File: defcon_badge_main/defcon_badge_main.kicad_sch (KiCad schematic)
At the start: 2 parts, among them U1 TPS61023DRLR, U2 TPS61023DRLR

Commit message: progress from 2_21_26
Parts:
- removed U1, U2: TPS61023DRLR, TPS61023DRLR:SOT563-ORI, symbol TPS61023DRLR:TPS61023DRLR
- added BT1: Battery, symbol Device:Battery
- added J2: ~, joystick:joystick, symbol joystick:joystick
- added M1, M2, M3: Stepper_Motor_bipolar, symbol Motor:Stepper_Motor_bipolar
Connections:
- net GND: now also BT1.2 (-)
- new net 3v3_power/VBAT: BT1.1 (+)
- new net motor_driver/OUT1A: M1.2 (-)
- new net motor_driver/OUT1B: M1.1
- new net motor_driver/OUT2A: M1.3
- new net motor_driver/OUT2B: M1.4
- new net motor_driver1/OUT1A: M2.2 (-)
- new net motor_driver1/OUT1B: M2.1
- new net motor_driver1/OUT2A: M2.3
- new net motor_driver1/OUT2B: M2.4
- new net motor_driver2/OUT1A: M3.2 (-)
- new net motor_driver2/OUT1B: M3.1
- new net motor_driver2/OUT2A: M3.3
- new net motor_driver2/OUT2B: M3.4
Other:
- added sheet 3v3_power (power_regulator.kicad_sch)
- added sheet 5v_power (power_reg_5v.kicad_sch)
- added sheet esp32 (esp32.kicad_sch)
- added sheet motor_driver (motor_drivers.kicad_sch)
- added sheet motor_driver1 (motor_drivers.kicad_sch)
- added sheet motor_driver2 (motor_drivers.kicad_sch)

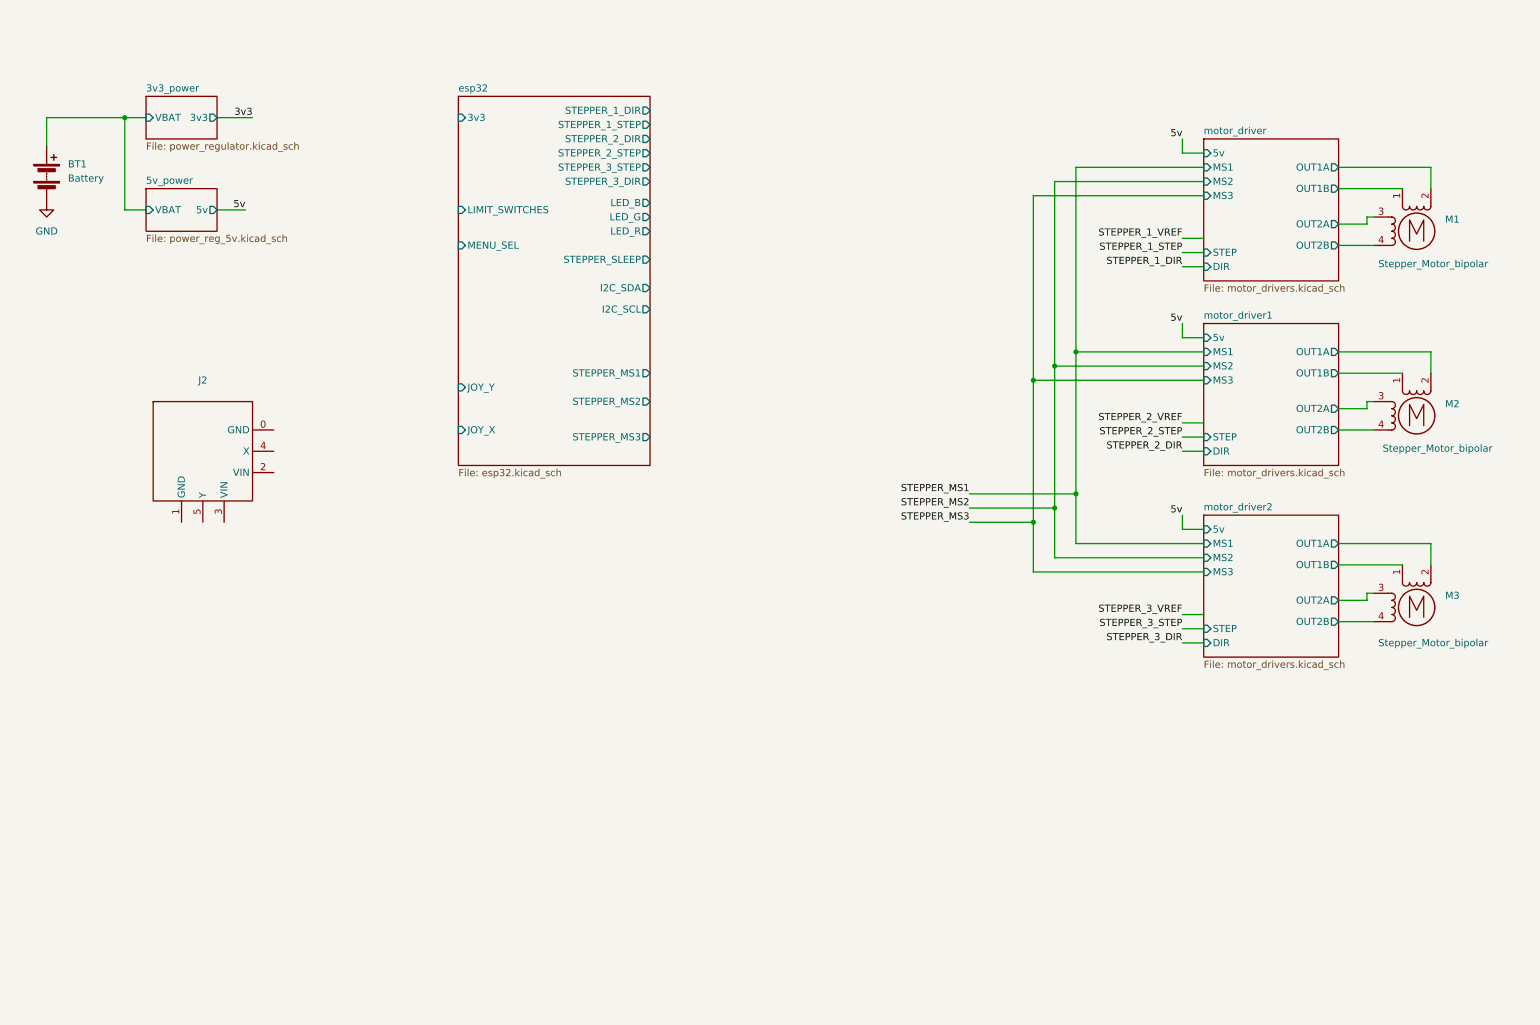
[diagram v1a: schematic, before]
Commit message: ESP32 test board layout
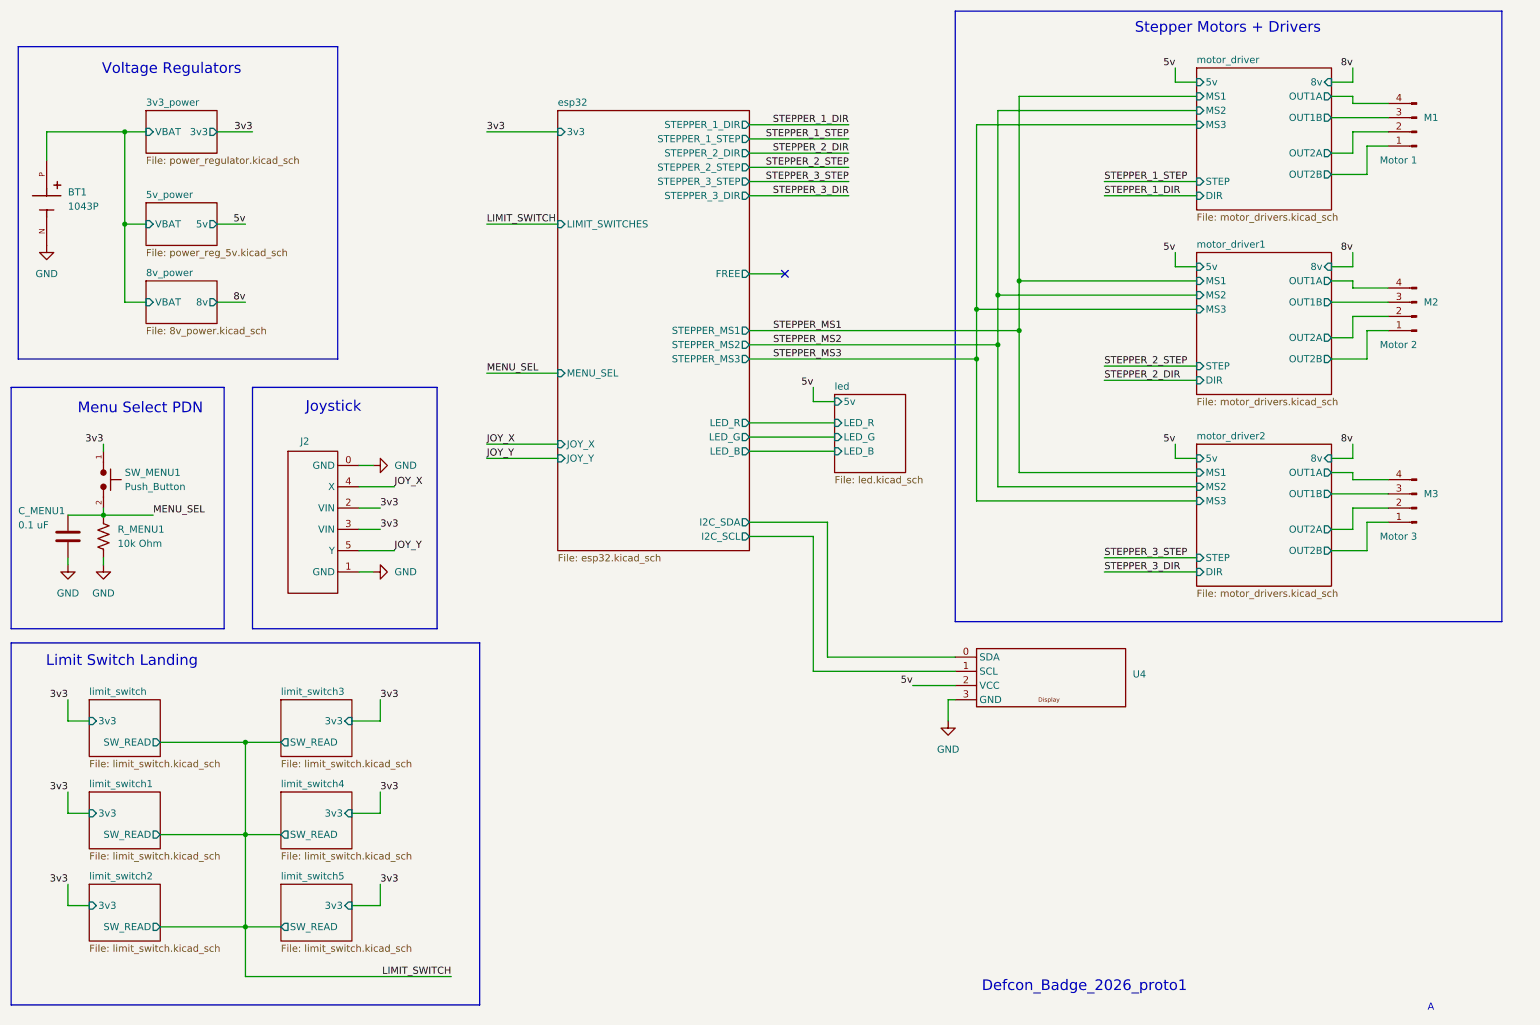
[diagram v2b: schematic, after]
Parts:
- removed BT1: Battery, symbol Device:Battery
- removed M1, M2, M3: Stepper_Motor_bipolar, symbol Motor:Stepper_Motor_bipolar
- added BT1: 1043P, 1043P:BAT_1043P, symbol 1043P:1043P
- added C_MENU1: 0.1 uF, PCM_SparkFun-Coil:0805, symbol Device:C
- added M1: Motor 1, joystick:motor_pins, symbol Connector:Conn_01x04_Pin
- added M2: Motor 2, joystick:motor_pins, symbol Connector:Conn_01x04_Pin
- added M3: Motor 3, joystick:motor_pins, symbol Connector:Conn_01x04_Pin
- added R_MENU1: 10k Ohm, PCM_SparkFun-Coil:0805, symbol Device:R_US
- added SW_MENU1: Push_Button, Button_Switch_SMD:SW_SPST_PTS645, symbol PCM_SL_Devices:Push_Button
- added U4: ~, display:display, symbol display:display
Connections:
- net 3v3: now also J2.2 (VIN), J2.3 (VIN), SW_MENU1.1
- net 3v3_power/VBAT: now also BT1.P
- net 5v: now also U4.2 (VCC)
- net GND: now also J2.0 (GND), J2.1 (GND), BT1.N, C_MENU1.1, R_MENU1.2, U4.3 (GND)
- net esp32/I2C_SCL: now also U4.1 (SCL)
- net esp32/I2C_SDA: now also U4.0 (SDA)
- net motor_driver/OUT1A: now also M1.4 (Pin_4)
- net motor_driver/OUT1B: now also M1.3 (Pin_3)
- net motor_driver/OUT2A: now also M1.2 (Pin_2)
- net motor_driver/OUT2B: now also M1.1 (Pin_1)
- net motor_driver1/OUT1A: now also M2.4 (Pin_4)
- net motor_driver1/OUT1B: now also M2.3 (Pin_3)
- net motor_driver1/OUT2A: now also M2.2 (Pin_2)
- net motor_driver1/OUT2B: now also M2.1 (Pin_1)
- net motor_driver2/OUT1A: now also M3.4 (Pin_4)
- net motor_driver2/OUT1B: now also M3.3 (Pin_3)
- net motor_driver2/OUT2A: now also M3.2 (Pin_2)
- net motor_driver2/OUT2B: now also M3.1 (Pin_1)
- net JOY_X: now reaches J2.4 (X)
- net JOY_Y: now reaches J2.5 (Y)
- new net MENU_SEL: C_MENU1.2, R_MENU1.1, SW_MENU1.2
- no-connect marks 0 -> 1
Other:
- added sheet 8v_power (8v_power.kicad_sch)
- added sheet led (led.kicad_sch)
- added sheet limit_switch (limit_switch.kicad_sch)
- added sheet limit_switch1 (limit_switch.kicad_sch)
- added sheet limit_switch2 (limit_switch.kicad_sch)
- added sheet limit_switch3 (limit_switch.kicad_sch)
- added sheet limit_switch4 (limit_switch.kicad_sch)
- added sheet limit_switch5 (limit_switch.kicad_sch)
- sheet esp32 ports: added FREE; removed STEPPER_SLEEP
- sheet motor_driver ports: added 8v; removed none
- sheet motor_driver1 ports: added 8v; removed none
- sheet motor_driver2 ports: added 8v; removed none
- note added: "A"
- note added: "Defcon_Badge_2026_proto1"
- note added: "Joystick"
- note added: "Limit Switch Landing"
- note added: "Menu Select PDN"
- note added: "Stepper Motors + Drivers"
- note added: "Voltage Regulators"
- moved on the sheet: J2

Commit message: more layout
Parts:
- C_MENU1, R_MENU1: footprint PCM_SparkFun-Coil:0805 -> joystick:R_0805_2012Metric_Pad1.20x1.40mm_HandSolder_MINE
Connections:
- net 3v3_power/VBAT renamed VBAT
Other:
- removed sheet limit_switch1
- removed sheet limit_switch2
- removed sheet limit_switch3
- removed sheet limit_switch4
- removed sheet limit_switch5

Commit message: moar layout
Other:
- sheet esp32 ports: added 5v; removed none
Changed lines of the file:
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@@
+	(wire
+		(pts
+			(xy 100.33 44.45) (xy 113.03 44.45)
+		)
+		(stroke
+			(width 0)
+			(type default)
+		)
+	)
 	(wire
 		(pts
@@
 	(label "MENU_SEL"
 		(at 100.33 80.01 0)
+		(effects
+			(font
+				(size 1.27 1.27)
+			)
+			(justify left bottom)
+		)
+	)
+	(label "5v"
+		(at 100.33 44.45 0)
 		(effects
 			(font
@@
 		(property "Component Class" ""
 			(at -12.7 -11.43 0)
+			(effects
+				(font
+					(size 1.27 1.27)
+					(italic yes)
+				)
+			)
+		)
+	)
+	(netclass_flag ""
+		(length 2.54)
+		(shape round)
+		(at 105.41 44.45 0)
+		(fields_autoplaced yes)
+		(effects
+			(font
+				(size 1.27 1.27)
+			)
+			(justify left bottom)
+		)
+		(property "Netclass" "5v"
+			(at 106.1085 41.91 0)
+			(effects
+				(font
+					(size 1.27 1.27)
+				)
+				(justify left)
+			)
+		)
+		(property "Component Class" ""
+			(at 39.37 -19.05 0)
 			(effects
 				(font
@@
 			)
 		)
+		(pin "5v" input
+			(at 113.03 44.45 180)
+			(effects
+				(font
+					(size 1.27 1.27)
+				)
+				(justify left)
+			)
+		)

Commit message: done?
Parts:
- removed BT1: 1043P, 1043P:BAT_1043P, symbol 1043P:1043P
- added BT2: BK-18650-PC2, BK-18650-PC2:BAT_BK-18650-PC2, symbol BK-18650-PC2:BK-18650-PC2
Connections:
- net GND: now also BT2.-
- net VBAT: now also BT2.+

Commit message: added component parts and modifications
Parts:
- BT2, J2, SW_MENU1, U4: now not fitted
- C_MENU1: footprint joystick:R_0805_2012Metric_Pad1.20x1.40mm_HandSolder_MINE -> joystick:R_0402_1005Metric_Pad0.72x0.64mm_HandSolder_MINE; MPN (none) -> GMC10X7R104M16NTD; Rating (none) -> 16V
- R_MENU1: value 10k Ohm -> 10 kOhm; MPN (none) -> RM10F1002CT; TOL (none) -> 1%
